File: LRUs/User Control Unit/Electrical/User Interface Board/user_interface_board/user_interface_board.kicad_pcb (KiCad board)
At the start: 2 copper layers, 59 x 110 mm, 18 parts, among them J1 S3B-PH-K-S, J10 S4B-PH-K-S, J11 S4B-PH-K-S, J12 S4B-PH-K-S, J13 S12B-PH-K-S, J2 S3B-PH-K-S, J3 S3B-PH-K-S, J4 S3B-PH-K-S, J5 S2B-PH-K-S, J6 S2B-PH-K-S, J7 S2B-PH-K-S, J8 S4B-PH-K-S, J9 S4B-PH-K-S, U1 LP5012PWR

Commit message: Commit
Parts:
- removed U1: LP5012PWR, footprints:TSSOP_012PWR_TEX
- added G***: LOGO, LOGO, F.Cu at (151.8, 76.6)
- added G***: LOGO, LOGO, F.Cu at (140.4, 105.6)
- added H5: MountingHole_Pad, MountingHole:MountingHole_2.2mm_M2_DIN965_Pad, F.Cu at (148.7, 55.0)
- added R92: 10k, footprints:R_0603_1608Metric, F.Cu at (130.4, 78.0)
- added R93: 10k, footprints:R_0603_1608Metric, F.Cu at (130.4, 68.0)
- added U2: LP5012PWR, footprints:TSSOP_012PWR_TEX, F.Cu at (159.0, 100.1)
- moved J10 35.0 mm to (170.6, 118.0)
- moved J4 30.0 mm to (124.5, 48.0)
- moved J1 30.0 mm to (124.5, 78.0)
- moved J12 27.0 mm to (170.6, 88.0)
- moved J2 10.0 mm to (124.5, 68.0)
- moved J3 10.0 mm to (124.5, 58.0)
- moved J11 4.00 mm to (170.6, 103.0)
- moved J13 1.00 mm to (146.0, 140.6)
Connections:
- J1 pad 1: unconnected-(J1-Pin_1-Pad1) -> Net-(J1-Pin_1)
- J1 pad 2: unconnected-(J1-Pin_2-Pad2) -> Net-(J1-Pin_2)
- J1 pad 3: unconnected-(J1-Pin_3-Pad3) -> GND
- J10 pad 1: unconnected-(J10-Pin_1-Pad1) -> +5V
- J10 pad 2: unconnected-(J10-Pin_2-Pad2) -> /top level/LED driver/OUT0
- J10 pad 3: unconnected-(J10-Pin_3-Pad3) -> /top level/LED driver/OUT1
- J10 pad 4: unconnected-(J10-Pin_4-Pad4) -> /top level/LED driver/OUT2
- J11 pad 1: unconnected-(J11-Pin_1-Pad1) -> +5V
- J11 pad 2: unconnected-(J11-Pin_2-Pad2) -> /top level/LED driver/OUT3
- J11 pad 3: unconnected-(J11-Pin_3-Pad3) -> /top level/LED driver/OUT4
- J11 pad 4: unconnected-(J11-Pin_4-Pad4) -> /top level/LED driver/OUT5
- J12 pad 1: unconnected-(J12-Pin_1-Pad1) -> +5V
- J12 pad 2: unconnected-(J12-Pin_2-Pad2) -> /top level/LED driver/OUT6
- J12 pad 3: unconnected-(J12-Pin_3-Pad3) -> /top level/LED driver/OUT7
- J12 pad 4: unconnected-(J12-Pin_4-Pad4) -> /top level/LED driver/OUT8
- J13 pad 1: +3V3 -> +5V
- J13 pad 10: unconnected-(J13-Pin_10-Pad10) -> GND
- J13 pad 11: unconnected-(J13-Pin_11-Pad11) -> Net-(J13-Pin_11)
- J13 pad 12: unconnected-(J13-Pin_12-Pad12) -> Net-(J13-Pin_12)
- J13 pad 5: unconnected-(J13-Pin_5-Pad5) -> /top level/I2C_SDA
- J13 pad 6: unconnected-(J13-Pin_6-Pad6) -> /top level/I2C_SCL
- J13 pad 7: unconnected-(J13-Pin_7-Pad7) -> /top level/launch circuit/ARMED_STAT
- J13 pad 8: unconnected-(J13-Pin_8-Pad8) -> /top level/launch circuit/LAUNCH_STAT
- J13 pad 9: unconnected-(J13-Pin_9-Pad9) -> Net-(J1-Pin_2)
- J2 pad 1: unconnected-(J2-Pin_1-Pad1) -> Net-(J2-Pin_1)
- J2 pad 2: unconnected-(J2-Pin_2-Pad2) -> Net-(J2-Pin_2)
- J2 pad 3: unconnected-(J2-Pin_3-Pad3) -> GND
- J3 pad 1: unconnected-(J3-Pin_1-Pad1) -> Net-(J2-Pin_2)
- J3 pad 2: unconnected-(J3-Pin_2-Pad2) -> Net-(J13-Pin_11)
- J3 pad 3: unconnected-(J3-Pin_3-Pad3) -> GND
- J4 pad 1: unconnected-(J4-Pin_1-Pad1) -> Net-(J2-Pin_2)
- J4 pad 2: unconnected-(J4-Pin_2-Pad2) -> Net-(J13-Pin_12)
- J4 pad 3: unconnected-(J4-Pin_3-Pad3) -> GND
- J5 pad 1: unconnected-(J5-Pin_1-Pad1) -> /top level/launch circuit/SAFE_LED+
- J5 pad 2: unconnected-(J5-Pin_2-Pad2) -> /top level/launch circuit/SAFE_LED-
- J6 pad 2: unconnected-(J6-Pin_2-Pad2) -> /top level/launch circuit/ARM_SW-
- J8 pad 1: unconnected-(J8-Pin_1-Pad1) -> +3V3
- J8 pad 2: unconnected-(J8-Pin_2-Pad2) -> /top level/I2C_SCL
- J8 pad 3: unconnected-(J8-Pin_3-Pad3) -> /top level/I2C_SDA
- J8 pad 4: unconnected-(J8-Pin_4-Pad4) -> GND
- J9 pad 4: unconnected-(J9-Pin_4-Pad4) -> GND
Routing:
- net Net-(J13-Pin_12): track 0.00 -> 110.7 mm
- net Net-(J13-Pin_11): track 0.00 -> 97.8 mm
- net GND: track 0.00 -> 87.6 mm
- net Net-(J1-Pin_2): track 0.00 -> 81.4 mm
- net /top level/LED driver/OUT0: track 0.00 -> 23.0 mm
- net /top level/I2C_SCL: track 0.00 -> 22.7 mm
- net /top level/LED driver/OUT8: track 0.00 -> 21.3 mm
- net /top level/LED driver/OUT7: track 0.00 -> 20.4 mm
- net /top level/I2C_SDA: track 0.00 -> 20.4 mm
- net /top level/LED driver/OUT6: track 0.00 -> 19.0 mm
- net /top level/LED driver/OUT1: track 0.00 -> 16.0 mm
- net /top level/LED driver/OUT2: track 0.00 -> 14.1 mm
- net /top level/LED driver/OUT5: track 0.00 -> 10.3 mm
- net Net-(J2-Pin_2): track 0.00 -> 10.2 mm
- net /top level/LED driver/OUT4: track 0.00 -> 9.76 mm
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- added copper zone on F.Cu, net GND
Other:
- copper layers 2 -> 4
- board text added: "EMERALD"
- board text added: "REV A"

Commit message: interface board schematic
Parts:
- removed R92, R93: 10k, footprints:R_0603_1608Metric
- added C1: 1uF, Capacitor_SMD:C_0402_1005Metric, F.Cu at (101.8, 93.3)
- added C2: 1uF, Capacitor_SMD:C_0402_1005Metric, F.Cu at (101.8, 95.3)
- added C3: 0.1uF, Capacitor_SMD:C_0402_1005Metric, F.Cu at (101.8, 97.2)
- added D1: Green, LED_SMD:LED_0603_1608Metric, F.Cu at (95.5, 83.3)
- added D2: Blue, LED_SMD:LED_0603_1608Metric, F.Cu at (95.5, 85.9)
- added D3: Red, LED_SMD:LED_0603_1608Metric, F.Cu at (95.5, 88.5)
- added D4: PESD5V0H1BSF, Diode_SMD:Nexperia_DSN0603-2_0.6x0.3mm_P0.4mm, F.Cu at (104.3, 87.8)
- added D5: PESD5V0H1BSF, Diode_SMD:Nexperia_DSN0603-2_0.6x0.3mm_P0.4mm, F.Cu at (104.3, 89.5)
- added FB1: GZ1608D601TF, Inductor_SMD:L_0603_1608Metric, F.Cu at (105.2, 83.3)
- added FB2: GZ1608D601TF, Inductor_SMD:L_0603_1608Metric, F.Cu at (105.2, 85.8)
- added Q1: AO3401A, Package_TO_SOT_SMD:SOT-23, F.Cu at (95.9, 92.0)
- added R1: 470, Resistor_SMD:R_0402_1005Metric, F.Cu at (92.0, 83.0)
- added R10: 4.7k, Resistor_SMD:R_0402_1005Metric, F.Cu at (101.8, 85.0)
- added R11: 10k, Resistor_SMD:R_0402_1005Metric, F.Cu at (101.8, 87.0)
- added R12: 10k, Resistor_SMD:R_0402_1005Metric, F.Cu at (101.8, 89.0)
- added R2: 470, Resistor_SMD:R_0402_1005Metric, F.Cu at (92.0, 85.0)
- added R3: 10k, Resistor_SMD:R_0402_1005Metric, F.Cu at (92.0, 87.0)
- added R4: 10k, Resistor_SMD:R_0402_1005Metric, F.Cu at (92.0, 89.0)
- added R5: 470, Resistor_SMD:R_0402_1005Metric, F.Cu at (92.0, 91.0)
- added R6: 470, Resistor_SMD:R_0402_1005Metric, F.Cu at (92.0, 92.9)
- added R7: 470, Resistor_SMD:R_0402_1005Metric, F.Cu at (92.0, 94.9)
- added R8: 10k, Resistor_SMD:R_0402_1005Metric, F.Cu at (104.6, 93.3)
- added R9: 4.7k, Resistor_SMD:R_0402_1005Metric, F.Cu at (101.8, 83.0)
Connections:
- J13 pad 10: GND -> Net-(J13-Pin_10)
- J13 pad 7: /top level/launch circuit/ARMED_STAT -> /top level/launch circuit/ARMED_LED+
- J13 pad 8: /top level/launch circuit/LAUNCH_STAT -> /top level/launch circuit/BUTTON_NO
- J2 pad 2: Net-(J2-Pin_2) -> Net-(J13-Pin_10)
- J3 pad 1: Net-(J2-Pin_2) -> Net-(J13-Pin_10)
- J4 pad 1: Net-(J2-Pin_2) -> Net-(J13-Pin_10)
- J6 pad 1: unconnected-(J6-Pin_1-Pad1) -> +5V
- J6 pad 2: /top level/launch circuit/ARM_SW- -> /top level/launch circuit/ARMED_LED+
- J7 pad 1: unconnected-(J7-Pin_1-Pad1) -> /top level/launch circuit/ARMED_LED+
- J7 pad 2: unconnected-(J7-Pin_2-Pad2) -> /top level/launch circuit/ARMED_LED-
- J8 pad 2: /top level/I2C_SCL -> /top level/SCL
- J8 pad 3: /top level/I2C_SDA -> /top level/SDA
- J9 pad 1: unconnected-(J9-Pin_1-Pad1) -> /top level/launch circuit/ARMED_LED+
- J9 pad 2: unconnected-(J9-Pin_2-Pad2) -> /top level/launch circuit/BUTTON_NO
- J9 pad 3: unconnected-(J9-Pin_3-Pad3) -> /top level/launch circuit/ARMED_LED+
- U2 pad 1: unconnected-(U2-ADDR0-Pad1) -> GND
- U2 pad 10: unconnected-(U2-VCAP-Pad10) -> Net-(U2-VCAP)
- U2 pad 18: unconnected-(U2-DGND-Pad18) -> GND
- U2 pad 2: unconnected-(U2-AGND-Pad2) -> GND
- U2 pad 3: unconnected-(U2-ADDR1-Pad3) -> GND
- U2 pad 4: unconnected-(U2-VCC-Pad4) -> +3V3
- U2 pad 5: unconnected-(U2-SDA-Pad5) -> /top level/SDA
- U2 pad 6: unconnected-(U2-PGND-Pad6) -> GND
- U2 pad 7: unconnected-(U2-SCL-Pad7) -> /top level/SCL
- U2 pad 8: unconnected-(U2-EN-Pad8) -> /top level/LED driver/LED_EN
- U2 pad 9: unconnected-(U2-IREF-Pad9) -> Net-(U2-IREF)
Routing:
- net Net-(J13-Pin_10): track 0.00 -> 97.8 mm
- net GND: track 87.6 -> 0.00 mm
- net +3V3: track 0.00 -> 49.1 mm
- net /top level/I2C_SCL: track 22.7 -> 0.00 mm
- net /top level/I2C_SDA: track 20.4 -> 0.00 mm
- net Net-(J2-Pin_2): track 10.2 -> 0.00 mm
- added copper zone on B.Cu, net GND
- added copper zone on In1.Cu, net GND
- added copper zone on In2.Cu, net GND
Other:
- board text removed: "REV A"

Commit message: interface pcb
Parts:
- removed D5: PESD5V0H1BSF, Diode_SMD:Nexperia_DSN0603-2_0.6x0.3mm_P0.4mm
- removed the G*** at (151.8, 76.6)
- added R13: 0, Resistor_SMD:R_0402_1005Metric, F.Cu at (151.2, 103.0)
- added TP1: LED_OUT9, TestPoint:TestPoint_Pad_D1.5mm, F.Cu at (156.0, 94.2)
- added TP2: LED_OUT10, TestPoint:TestPoint_Pad_D1.5mm, F.Cu at (158.9, 94.2)
- added TP3: LED_OUT11, TestPoint:TestPoint_Pad_D1.5mm, F.Cu at (161.7, 94.3)
- added TP4: LED_EN, TestPoint:TestPoint_Pad_D1.5mm, F.Cu at (155.0, 108.0)
- D1: value Green -> KT-0805G; footprint LED_SMD:LED_0603_1608Metric -> LED_SMD:LED_0805_2012Metric
- D2: value Blue -> KT-0805Y; footprint LED_SMD:LED_0603_1608Metric -> LED_SMD:LED_0805_2012Metric
- D3: value Red -> KT-0603R
- D4: value PESD5V0H1BSF -> RCLAMP0582N(ES); footprint Diode_SMD:Nexperia_DSN0603-2_0.6x0.3mm_P0.4mm -> Project Library:SON40P100X120X65-6N
- R7: value 470 -> 180
- R8: value 10k -> 12k
- U2: footprint footprints:TSSOP_012PWR_TEX -> Project Library:TSSOP_012PWR_TEX
- moved R4 81.3 mm to (166.5, 56.5), turned to 180 degrees
- moved R2 79.0 mm to (161.0, 46.6), turned to -90 degrees
- moved R9 71.5 mm to (155.2, 130.4), turned to 180 degrees
- moved FB1 70.6 mm to (154.7, 133.6), turned to -90 degrees
- moved D4 70.1 mm to (154.0, 137.3), turned to -90 degrees
- moved R10 68.2 mm to (152.7, 130.4), turned to 180 degrees
- moved FB2 67.7 mm to (153.2, 133.6), turned to 90 degrees
- moved R7 63.1 mm to (143.4, 58.4), turned to -90 degrees
- moved Q1 61.6 mm to (141.0, 50.2), turned to 180 degrees
- moved R3 59.7 mm to (142.0, 54.4), turned to -90 degrees
- moved R6 59.2 mm to (140.1, 58.5), turned to -90 degrees
- moved R1 56.4 mm to (135.0, 46.6), turned to -90 degrees
- moved R5 55.1 mm to (136.5, 58.5), turned to -90 degrees
- moved D3 55.0 mm to (143.4, 61.5), turned to 90 degrees
- moved C1 53.2 mm to (154.1, 103.1), turned to -90 degrees
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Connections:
- C1 pad 2: unconnected-(C1-Pad2) -> GND
- D4 pad 1: GND -> /top level/I2C_SCL
- U2 pad 22: unconnected-(U2-OUT9-Pad22) -> Net-(U2-OUT9)
- U2 pad 23: unconnected-(U2-OUT10-Pad23) -> Net-(U2-OUT10)
- U2 pad 24: unconnected-(U2-OUT11-Pad24) -> Net-(U2-OUT11)
- U2 pad 8: /top level/LED driver/LED_EN -> Net-(U2-EN)
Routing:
- net /top level/launch circuit/ARMED_LED+: track 0.00 -> 145.8 mm
- net /top level/launch circuit/BUTTON_NO: track 0.00 -> 121.9 mm, vias 0 -> 1
- net /top level/SDA: track 0.00 -> 51.1 mm, vias 0 -> 2
- net /top level/SCL: track 0.00 -> 47.9 mm
- net GND: track 0.00 -> 28.3 mm, vias 0 -> 15
- net +3V3: track 49.1 -> 24.3 mm, vias 0 -> 6
- net Net-(J13-Pin_10): track 97.8 -> 115.6 mm
- net Net-(U2-EN): track 0.00 -> 13.2 mm
- net /top level/launch circuit/SAFE_LED+: track 0.00 -> 8.68 mm
- net Net-(U2-OUT9): track 0.00 -> 7.40 mm
- net /top level/I2C_SCL: track 0.00 -> 7.01 mm
- net /top level/I2C_SDA: track 0.00 -> 6.54 mm
- net Net-(U2-OUT10): track 0.00 -> 4.65 mm
- net Net-(U2-IREF): track 0.00 -> 3.93 mm
- net +5V: track 0.00 -> 2.71 mm, vias 0 -> 2
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- added copper zone on In2.Cu, net +3V3
- added copper zone on In2.Cu, net +5V
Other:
- board text added: "+"
- board text added: "4"

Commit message: last update for review
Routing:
- net GND: track 28.3 -> 31.9 mm, vias 15 -> 217
- net Net-(J13-Pin_12): track 110.7 -> 108.6 mm
- net Net-(J1-Pin_2): track 81.4 -> 80.5 mm
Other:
- board text removed: "4"

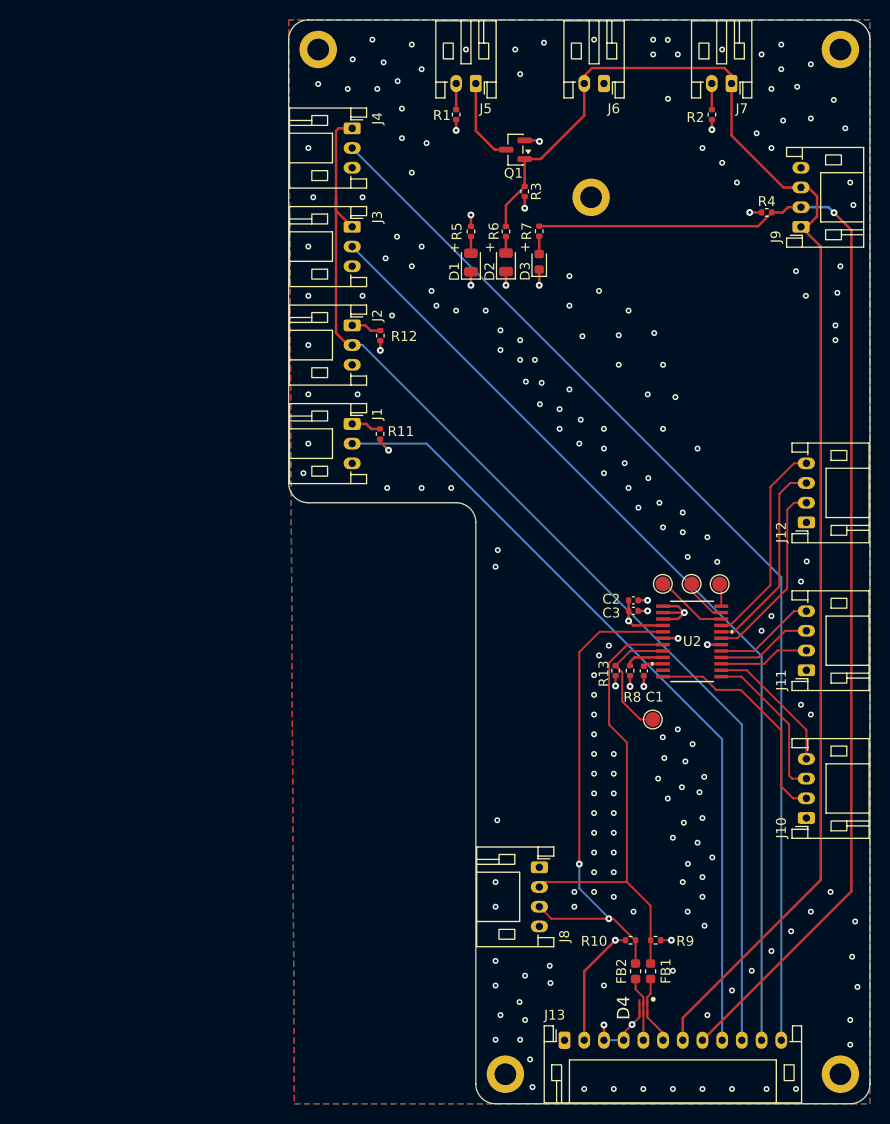
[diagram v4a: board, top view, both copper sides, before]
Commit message: fix drc & add level shifter
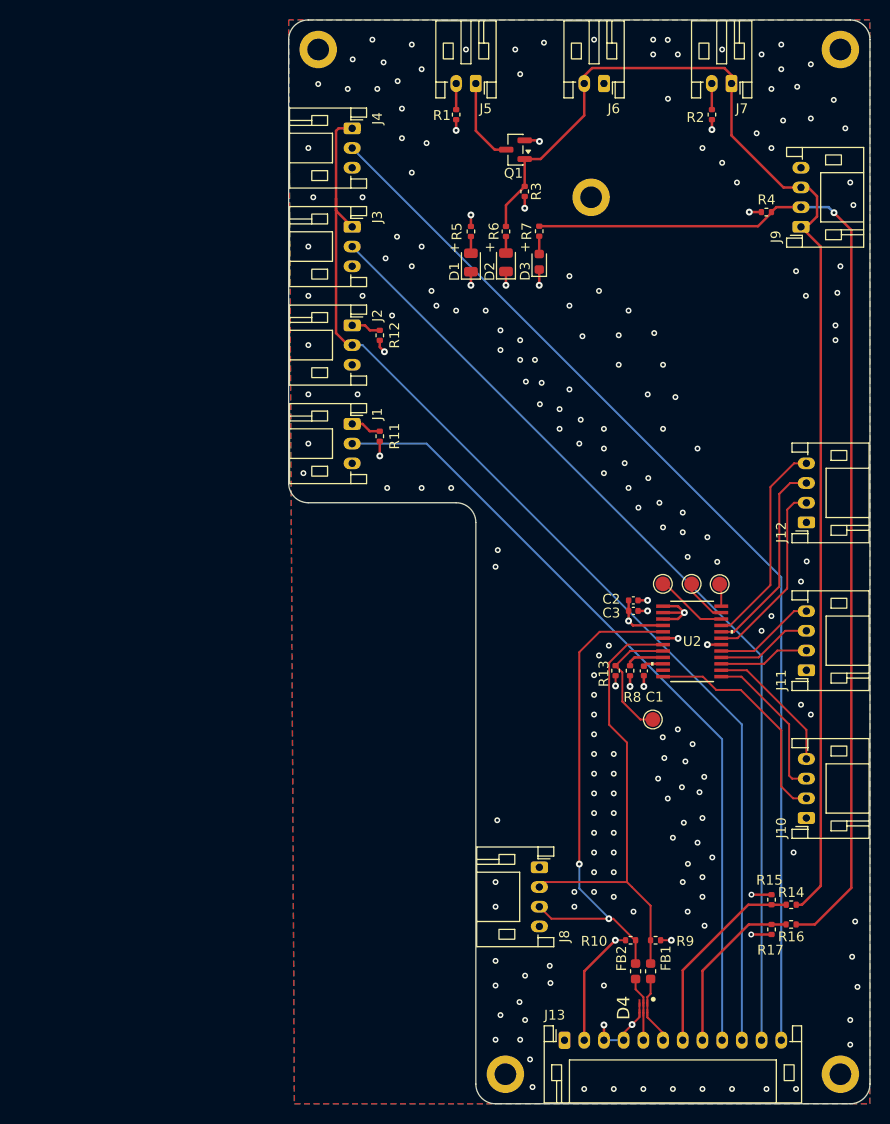
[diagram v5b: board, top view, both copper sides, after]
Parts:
- added R14: 1k, Resistor_SMD:R_0402_1005Metric, F.Cu at (169.0, 126.8)
- added R15: 2k, Resistor_SMD:R_0402_1005Metric, F.Cu at (167.0, 126.3)
- added R16: 1k, Resistor_SMD:R_0402_1005Metric, F.Cu at (169.0, 128.8)
- added R17: 2k, Resistor_SMD:R_0402_1005Metric, F.Cu at (167.0, 129.3)
- R7: value 180 -> 200
- moved R11 0.23 mm to (127.2, 79.2)
- moved R12 0.06 mm to (127.2, 69.0)
- moved R4 0.05 mm to (166.5, 56.5)
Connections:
- J13 pad 7: /top level/launch circuit/ARMED_LED+ -> /top level/launch circuit/ARMED_STAT
- J13 pad 8: /top level/launch circuit/BUTTON_NO -> /top level/launch circuit/LAUNCH_STAT
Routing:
- net /top level/launch circuit/ARMED_STAT: track 0.00 -> 20.4 mm
- net /top level/launch circuit/ARMED_LED+: track 145.8 -> 127.6 mm
- net /top level/launch circuit/LAUNCH_STAT: track 0.00 -> 17.5 mm
- net /top level/launch circuit/BUTTON_NO: track 121.9 -> 107.4 mm
- net GND: track 31.9 -> 36.0 mm, vias 217 -> 212
